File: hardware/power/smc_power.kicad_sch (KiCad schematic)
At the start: 56 parts, among them IC1 LM393DR2GH, J1 Screw_Terminal_Input, J2 Screw_Terminal_Output, Q2 P40B10SL, U1 TPS54360DDA, U2 TPS54360DDA, U3 AP2112K-3.3, U6 TL431D

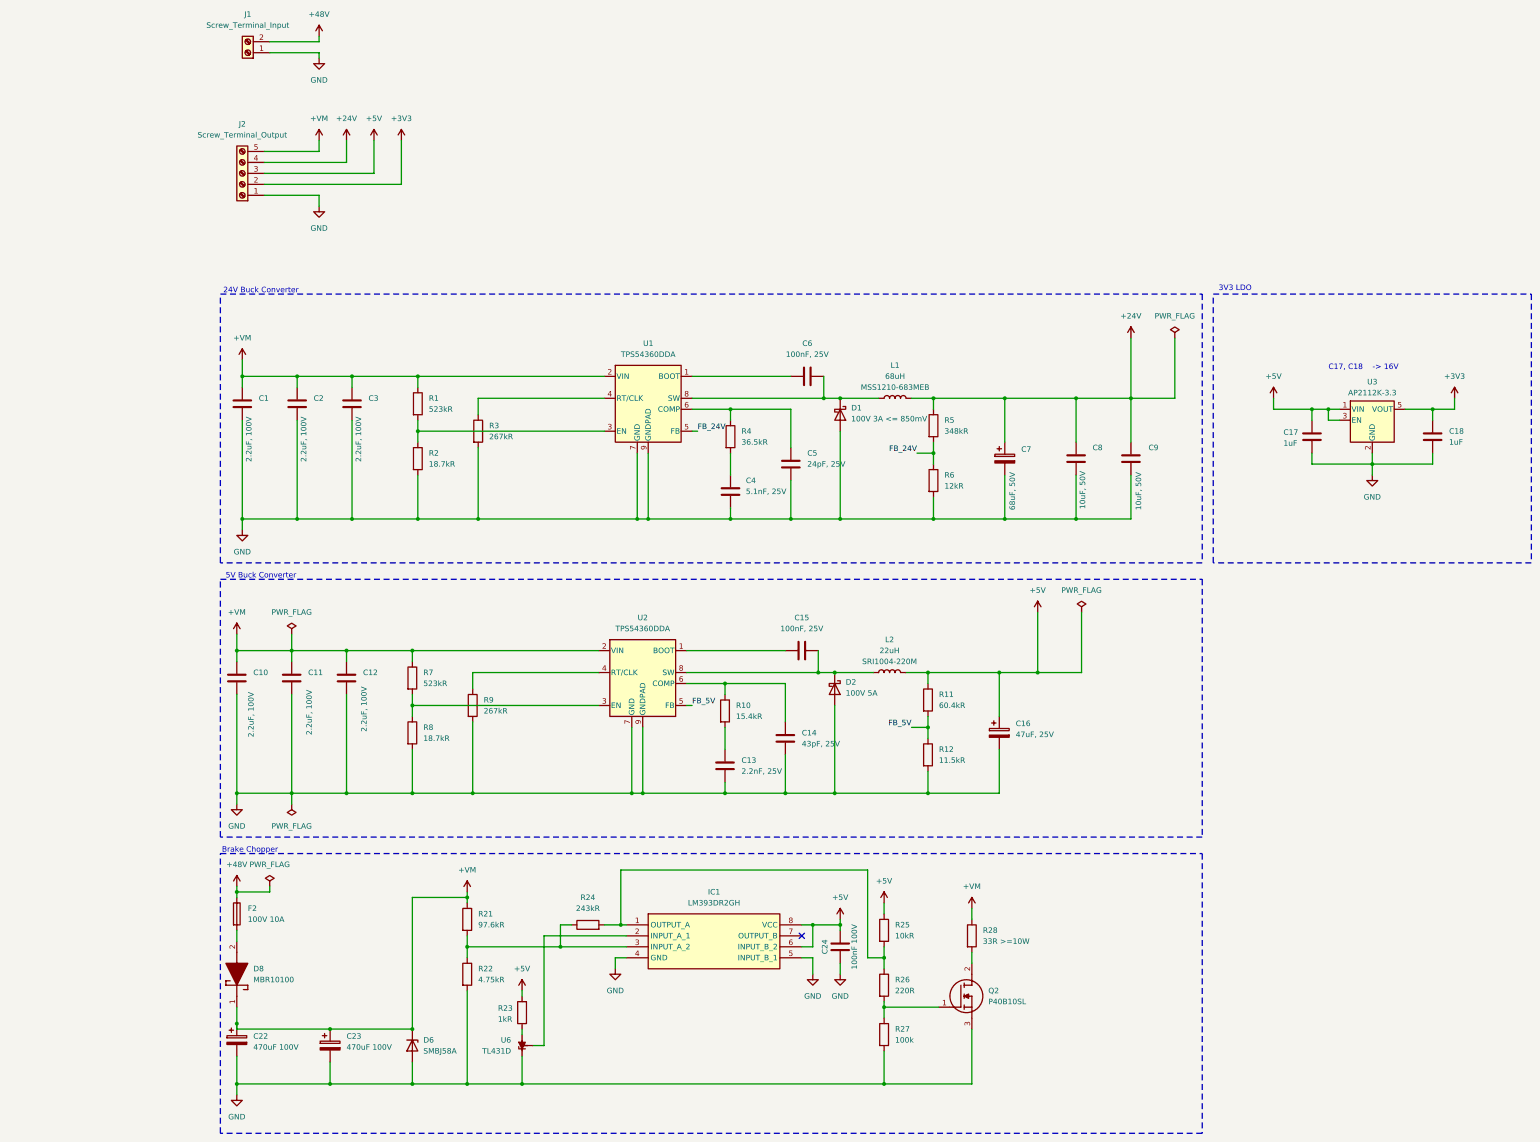
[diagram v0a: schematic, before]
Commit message: hw(power): add MCP1416 gate driver + 12V LDO for brake chopper Q2, 10R gate resistor, closes #31
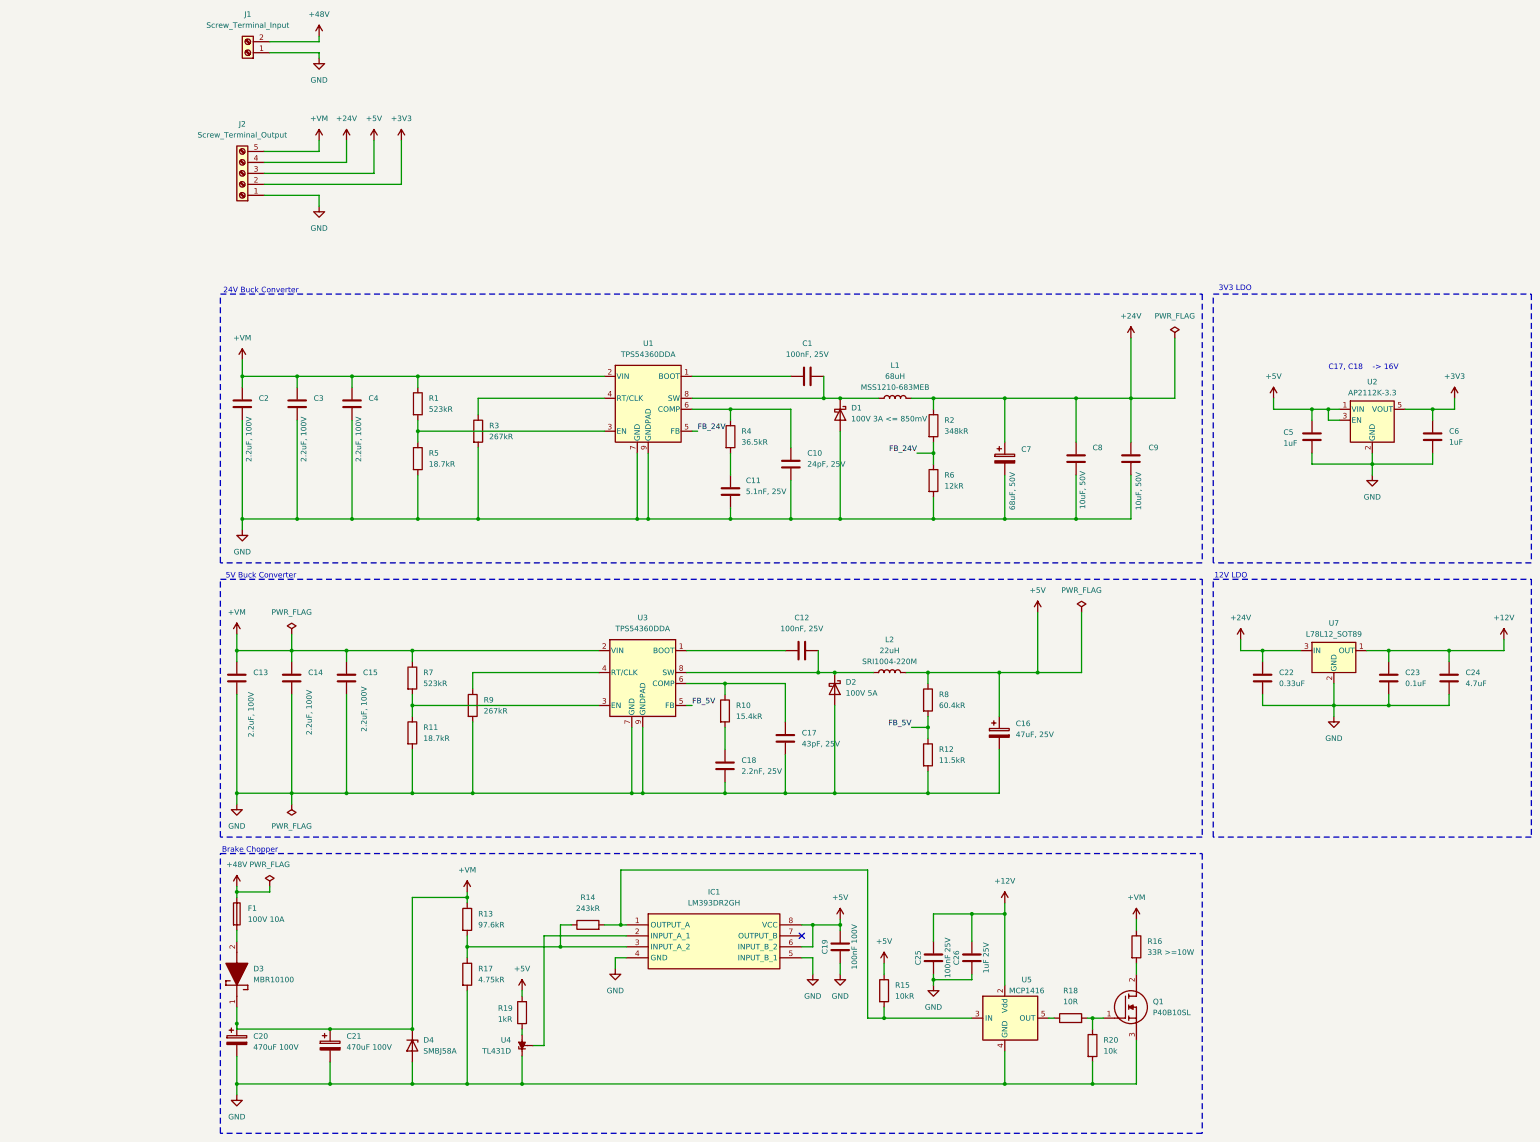
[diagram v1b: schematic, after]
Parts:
- removed R25: 10kR, Resistor_SMD:R_0805_2012Metric_Pad1.20x1.40mm_HandSolder, symbol Device:R
- removed U6: TL431D, Package_SO:SOIC-8_3.9x4.9mm_P1.27mm, symbol Reference_Voltage:TL431D
- added C22: 0.33uF, Package_TO_SOT_SMD:SOT-89-3, symbol Device:C
- added C23: 0.1uF, Package_TO_SOT_SMD:SOT-89-3, symbol Device:C
- added C24: 4.7uF, Package_TO_SOT_SMD:SOT-89-3, symbol Device:C
- added C25: 100nF 25V, Capacitor_SMD:C_0805_2012Metric_Pad1.18x1.45mm_HandSolder, symbol Device:C
- added C26: 1uF 25V, Capacitor_SMD:C_0805_2012Metric_Pad1.18x1.45mm_HandSolder, symbol Device:C
- added R15: 10kR, Resistor_SMD:R_0805_2012Metric_Pad1.20x1.40mm_HandSolder, symbol Device:R
- added U4: TL431D, Package_SO:SOIC-8_3.9x4.9mm_P1.27mm, symbol Reference_Voltage:TL431D
- added U5: MCP1416, Package_TO_SOT_SMD:SOT-23-5, symbol Driver_FET:MCP1416
- added U7: L78L12_SOT89, Package_TO_SOT_SMD:SOT-89-3, symbol Regulator_Linear:L78L12_SOT89
- R18: renamed from R26; value 220R -> 10R
- R20: renamed from R27; value 100k -> 10k
- renumbered C6 to C1, C5 to C10, C4 to C11, C15 to C12, C10 to C13, C11 to C14, C12 to C15, C14 to C17, C13 to C18, C24 to C19, C1 to C2, C22 to C20, C23 to C21, C2 to C3, C3 to C4, C17 to C5, C18 to C6, D8 to D3, D6 to D4, F2 to F1, Q2 to Q1, R8 to R11, R21 to R13, R24 to R14, R28 to R16, R22 to R17, R23 to R19, R5 to R2, R2 to R5, R11 to R8, U3 to U2, U2 to U3
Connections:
- net +24V: now also C22.1, U7.3 (IN)
- net +5V: now also R15.1
- net GND: now also C22.2, C23.2, C24.2, C25.1, C26.1, U4.1 (K), U5.4 (GND), U7.2 (GND)
- net at R19.1: now also U4.[2,3,6,7] (A)
- net at IC1.1 (OUTPUT_A), R14.2: now also R15.2, U5.3 (IN); no longer R18.1
- net at IC1.2 (INPUT_A_1): now also U4.8 (REF)
- new net: R18.1, U5.5 (OUT)
- new net +12V: C23.1, C24.1, C25.2, C26.2, U5.2 (Vdd), U7.1 (OUT)
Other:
- note added: "12V LDO"
- moved on the sheet: Q1, R16, R18, R20

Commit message: hw(power): RX24 50W brake resistor + SS510 flyback diode, closes #32
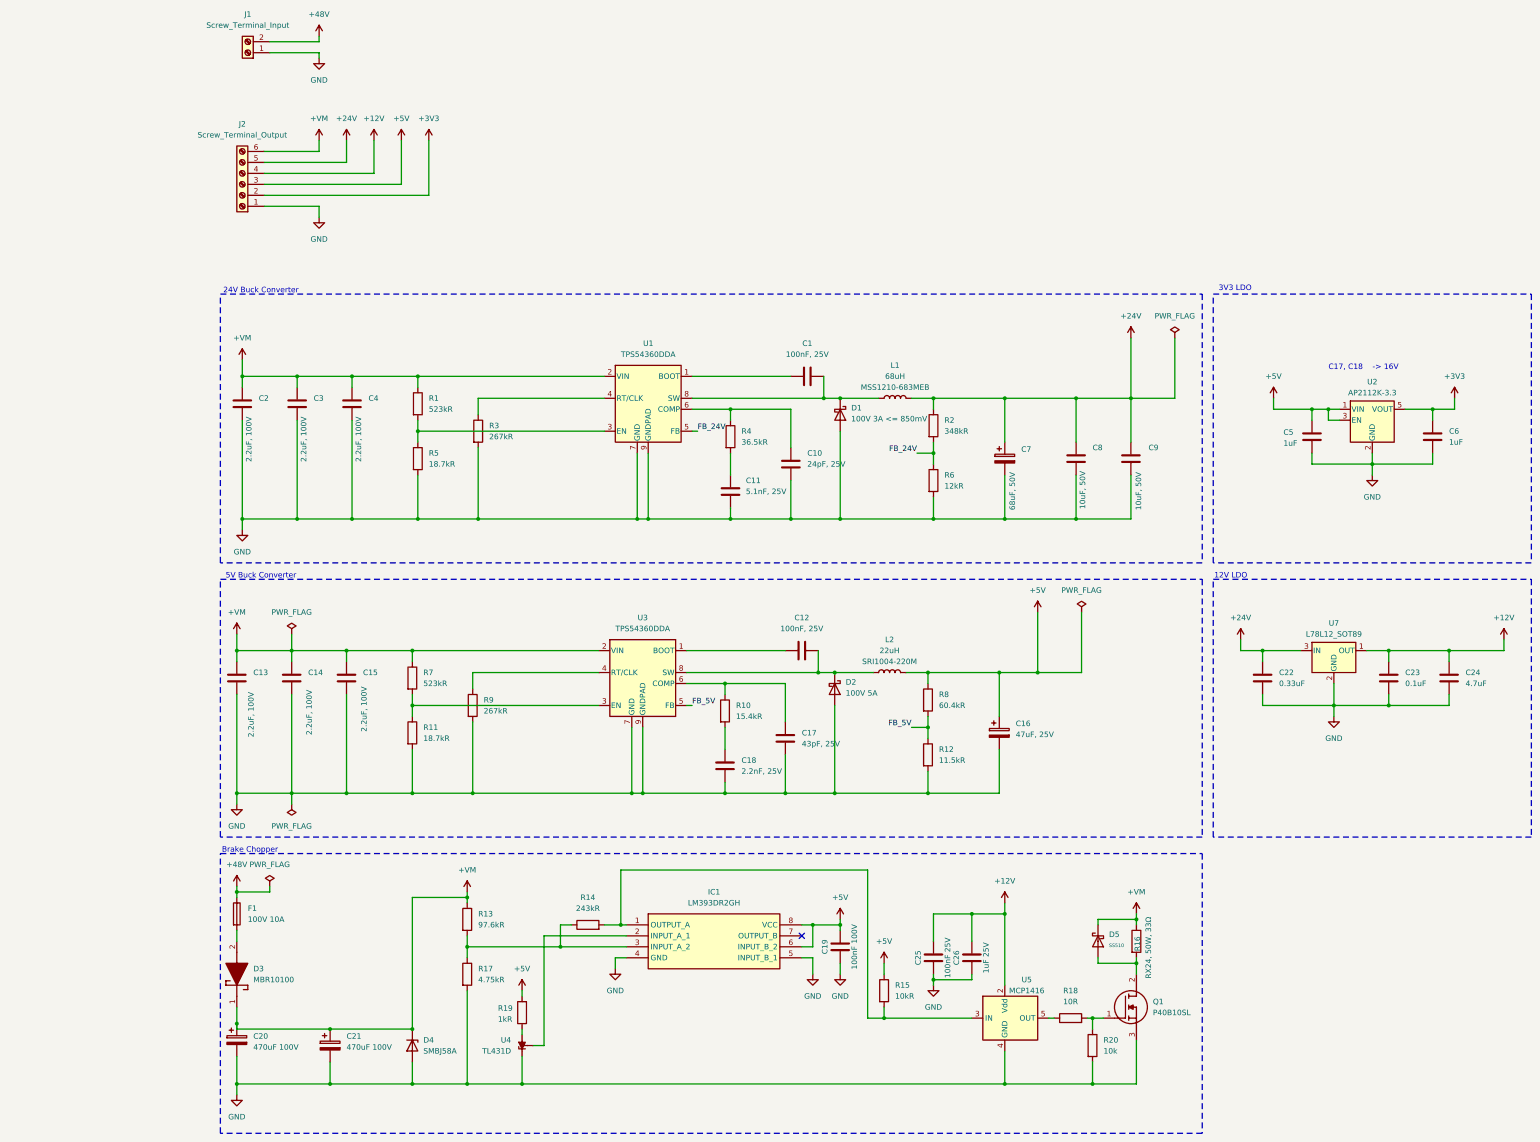
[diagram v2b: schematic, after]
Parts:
- removed J2: Screw_Terminal_Output, symbol Connector:Screw_Terminal_01x05
- added D5: SS510, PCM_JLCPCB:D_SMA, symbol PCM_JLCPCB-Diodes:Schottky,SS510
- added J2: Screw_Terminal_Output, TerminalBlock_Phoenix:TerminalBlock_Phoenix_MPT-0,5-6-2.54_1x06_P2.54mm_Horizontal, symbol Connector:Screw_Terminal_01x06
- R16: value 33R >=10W -> RX24, 50W, 33Ω
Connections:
- net +12V: now also J2.4 (Pin_4)
- net +24V: now also J2.5 (Pin_5)
- net +3V3: now also J2.2 (Pin_2)
- net +5V: now also J2.3 (Pin_3)
- net +VM: now also D5.1, J2.6 (Pin_6)
- net GND: now also J2.1 (Pin_1)
- net at Q1.2 (D), R16.2: now also D5.2
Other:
- moved on the sheet: R16

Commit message: hw(power): label SW/BOOT/FB nets, add SW_NODE/BOOT_NODE classes, ERC clean, closes #34
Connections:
- net SW_5V: now reaches C12.2, D2.1 (K), L2.1, U3.8 (SW)
- net BOOT_5V: now reaches C12.1, U3.1 (BOOT)
- net BOOT_24V: now reaches C1.1, U1.1 (BOOT)
- net SW_24V: now reaches C1.2, D1.1 (K), L1.1, U1.8 (SW)
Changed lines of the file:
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@@
+		)
+	)
+	(label "BOOT_5V"
+		(at 127 167.64 0)
+		(effects
+			(font
+				(size 1.27 1.27)
+			)
+			(justify left bottom)
+		)
+	)
+	(label "SW_24V"
+		(at 128.27 109.22 0)
+		(effects
+			(font
+				(size 1.27 1.27)
+			)
+			(justify left bottom)
 		)
 	)
@@
 		)
 	)
+	(label "SW_5V"
+		(at 127 172.72 0)
+		(effects
+			(font
+				(size 1.27 1.27)
+			)
+			(justify left bottom)
+		)
+	)
+	(label "BOOT_24V"
+		(at 128.27 104.14 0)
+		(effects
+			(font
+				(size 1.27 1.27)
+			)
+			(justify left bottom)
+		)
+	)

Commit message: hw(power): move +VM and SS510 into project library, SS510 footprint -> Diode_SMD:D_SMA (no machine-local libs)
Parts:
- D5: footprint PCM_JLCPCB:D_SMA -> Diode_SMD:D_SMA; symbol PCM_JLCPCB-Diodes:Schottky,SS510 -> Step Motor Controller:SS510
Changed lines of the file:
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@@
 	)
 	(symbol
-		(lib_id "power:+VM")
+		(lib_id "Step Motor Controller:+VM")
 		(at 21.59 163.83 0)
 		(unit 1)
@@
 	)
 	(symbol
-		(lib_id "power:+VM")
+		(lib_id "Step Motor Controller:+VM")
 		(at 74.93 223.52 0)
 		(unit 1)
@@
 	)
 	(symbol
-		(lib_id "power:+VM")
+		(lib_id "Step Motor Controller:+VM")
 		(at 40.64 49.53 0)
 		(unit 1)
@@
 	)
 	(symbol
-		(lib_id "PCM_JLCPCB-Diodes:Schottky,SS510")
+		(lib_id "Step Motor Controller:SS510")
 		(at 220.98 234.95 180)
 		(unit 1)
@@
 			)
 		)
-		(property "Footprint" "PCM_JLCPCB:D_SMA"
+		(property "Footprint" "Diode_SMD:D_SMA"
 			(at 222.758 234.95 90)
 			(hide yes)
@@
 	)
 	(symbol
-		(lib_id "power:+VM")
+		(lib_id "Step Motor Controller:+VM")
 		(at 22.86 100.33 0)
 		(unit 1)
@@
 	)
 	(symbol
-		(lib_id "power:+VM")
+		(lib_id "Step Motor Controller:+VM")
 		(at 229.87 228.6 0)
 		(unit 1)
